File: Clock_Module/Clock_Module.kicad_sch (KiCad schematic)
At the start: 22 parts, among them SW1 SW_Wuerth_450301014042, U1 74LS08, U2 LM555xN, U3 LM555xN, U4 LM555xN, U5 74LS32, U6 74LS04

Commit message: Checkpoint: cleaned up clock module. Made one schematic. Good stop point
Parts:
- removed C3, C4, C6: .01µF, Capacitor_THT:C_Disc_D5.0mm_W2.5mm_P2.50mm, symbol Device:C
- removed D1: LED, LED_THT:LED_D5.0mm, symbol Device:LED
- removed Push1: SW_Push, Button_Switch_THT:SW_PUSH_6mm_H4.3mm, symbol Switch:SW_Push
- removed R3: 1M, Resistor_THT:R_Axial_DIN0207_L6.3mm_D2.5mm_P5.08mm_Vertical, symbol Device:R
- removed R4, R5, R6, R7: 1K, Resistor_THT:R_Axial_DIN0207_L6.3mm_D2.5mm_P5.08mm_Vertical, symbol Device:R
- removed SW1: SW_Wuerth_450301014042, MyFootPrints:SW_Slide-Jameco-SS-12E17-G020, symbol Switch:SW_Wuerth_450301014042
- removed U1: 74LS08, MyFootPrints:SN74LS08N, symbol 74xx:74LS08
- removed U2, U3, U4: LM555xN, Package_DIP:DIP-8_W7.62mm, symbol Timer:LM555xN
- removed U5: 74LS32, MyFootPrints:SN74LS32N, symbol 74xx:74LS32
- removed U6: 74LS04, MyFootPrints:SN74LS04N, symbol 74xx:74LS04
- added C10, C8, C9: .01µF, Capacitor_THT:C_Disc_D5.0mm_W2.5mm_P2.50mm, symbol Device:C
- added D2: LED, LED_THT:LED_D5.0mm, symbol Device:LED
- added J2: Barrel_Jack, symbol Connector:Barrel_Jack
- added Push2: SW_Push, Button_Switch_THT:SW_PUSH_6mm_H4.3mm, symbol Switch:SW_Push
- added R10, R11, R12, R14: 1K, Resistor_THT:R_Axial_DIN0207_L6.3mm_D2.5mm_P5.08mm_Vertical, symbol Device:R
- added R13: 1M, Resistor_THT:R_Axial_DIN0207_L6.3mm_D2.5mm_P5.08mm_Vertical, symbol Device:R
- added SW2: SW_Wuerth_450301014042, MyFootPrints:SW_Slide-Jameco-SS-12E17-G020, symbol Switch:SW_Wuerth_450301014042
- added U1, U11, U12: LM555xN, Package_DIP:DIP-8_W7.62mm, symbol Timer:LM555xN
- added U7: 74LS08, MyFootPrints:SN74LS08N, symbol 74xx:74LS08
- added U8: 74LS32, MyFootPrints:SN74LS32N, symbol 74xx:74LS32
- added U9: 74LS04, MyFootPrints:SN74LS04N, symbol 74xx:74LS04
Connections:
- net 5V: now also J2.1, R13.1, R14.2, SW2.1 (B), U1.4 (R), U1.8 (VCC), U11.8 (VCC), U12.4 (R), U12.8 (VCC), U7.14 (VCC), U8.14 (VCC), U9.14 (VCC)
- net CLK: now also D2.2 (A), U7.8, U9.5
- net GND: now also C10.1, C8.1, C9.1, J2.2, Push2.1, R10.1, R11.2, R12.2, U1.1 (GND), U1.5 (CV), U11.1 (GND), U11.6 (THR), U11.7 (DIS), U12.1 (GND), U7.7 (GND), U8.7 (GND), U9.7 (GND)
- net astable_out: now also U1.3 (Q), U7.1
- net bistable_out: now also U11.3 (Q), U7.2, U9.1
- net monostable_out: now also U12.3 (Q), U7.5
- net ~{CLK}: now also U9.6
- net at POT1.1: no longer R2.2
- net at POT1.2: now also R2.2
- net at C1.1, POT1.3: now also U1.2 (TR), U1.6 (THR)
- net at R1.1, R2.1: now also U1.7 (DIS)
- new net: D2.1 (K), R12.1
- new net: Push2.2, R14.1, U12.2 (TR)
- new net: U7.3, U8.1
- new net: U7.4, U9.2
- new net: R11.1, SW2.3 (A), U11.2 (TR)
- new net: R10.2, SW2.2 (C), U11.4 (R)
- new net: C8.2, U11.5 (CV)
- new net: U7.6, U8.2
- new net: U7.10, U9.4
- new net: C9.2, R13.2, U12.6 (THR), U12.7 (DIS)
- new net: C10.2, U12.5 (CV)
- new net: U7.9, U8.3
- new net halt: U9.3
- no-connect marks 20 -> 21
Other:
- note added: "Remove later"
- note removed: "Change to HLT"

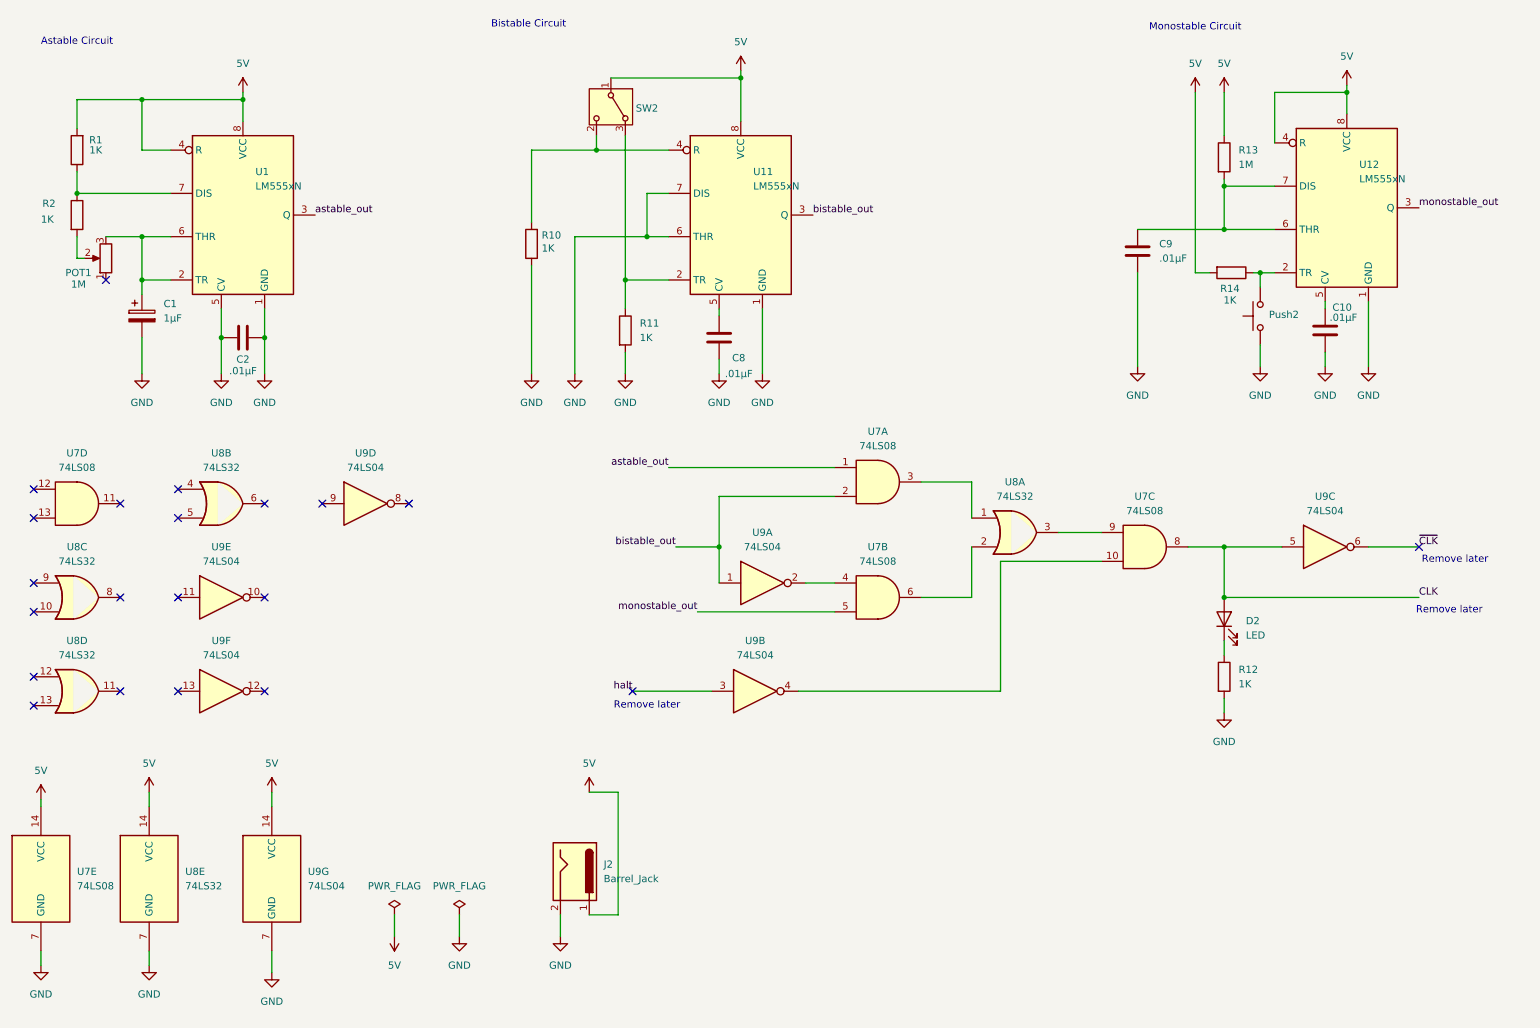
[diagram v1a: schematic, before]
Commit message: Updated Schematic to PC104 standards, updated Simulation for intel-quartus, updated PCB constraints, and edited board layout
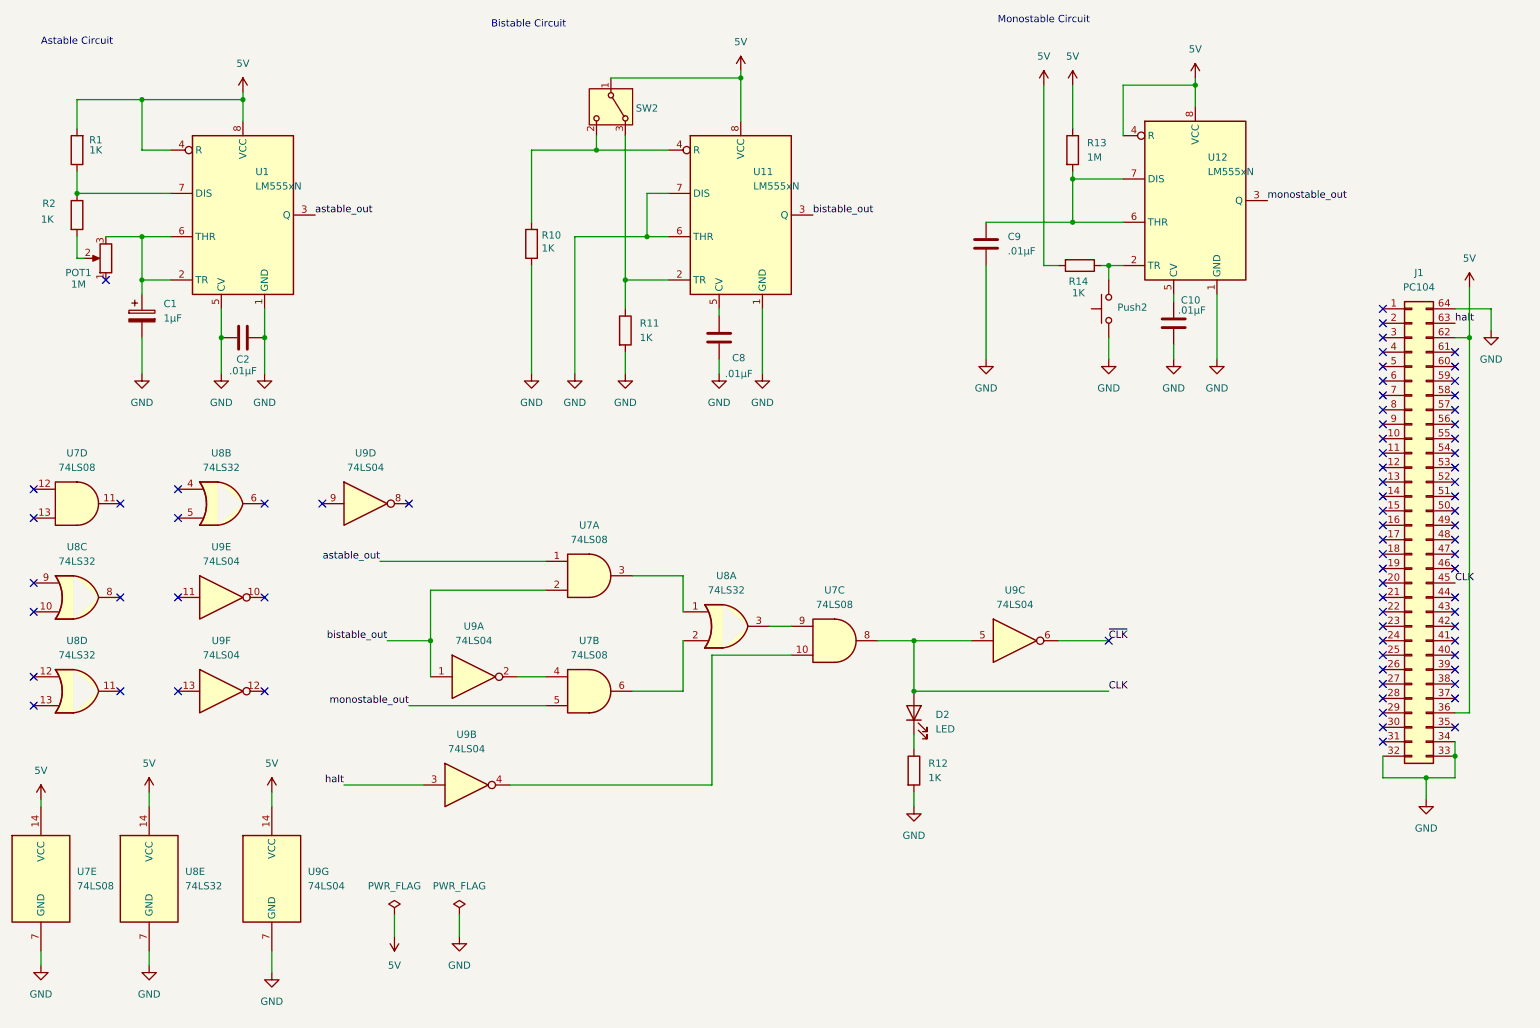
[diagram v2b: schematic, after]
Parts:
- removed J2: Barrel_Jack, symbol Connector:Barrel_Jack
- added J1: PC104, Connector_PinSocket_2.54mm:PinSocket_2x32_P2.54mm_Vertical, symbol Connector_Generic:Conn_02x32_Counter_Clockwise
- D2: footprint LED_THT:LED_D5.0mm -> LED_THT:LED_D5.0mm_Horizontal_O1.27mm_Z3.0mm
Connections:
- net 5V: now also J1.36 (Pin_36), J1.62 (Pin_62)
- net CLK: now also J1.45 (Pin_45)
- net GND: now also J1.32 (Pin_32), J1.33 (Pin_33), J1.34 (Pin_34), J1.64 (Pin_64)
- net halt: now also J1.63 (Pin_63)
- no-connect marks 21 -> 76
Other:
- note removed: "Remove later"
- moved on the sheet: C10, C9, D2, Push2, R12, R13, R14, U12, U7A, U7B, U7C, U8A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

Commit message: partially complete pcb and updated schematic with bypass capacitors
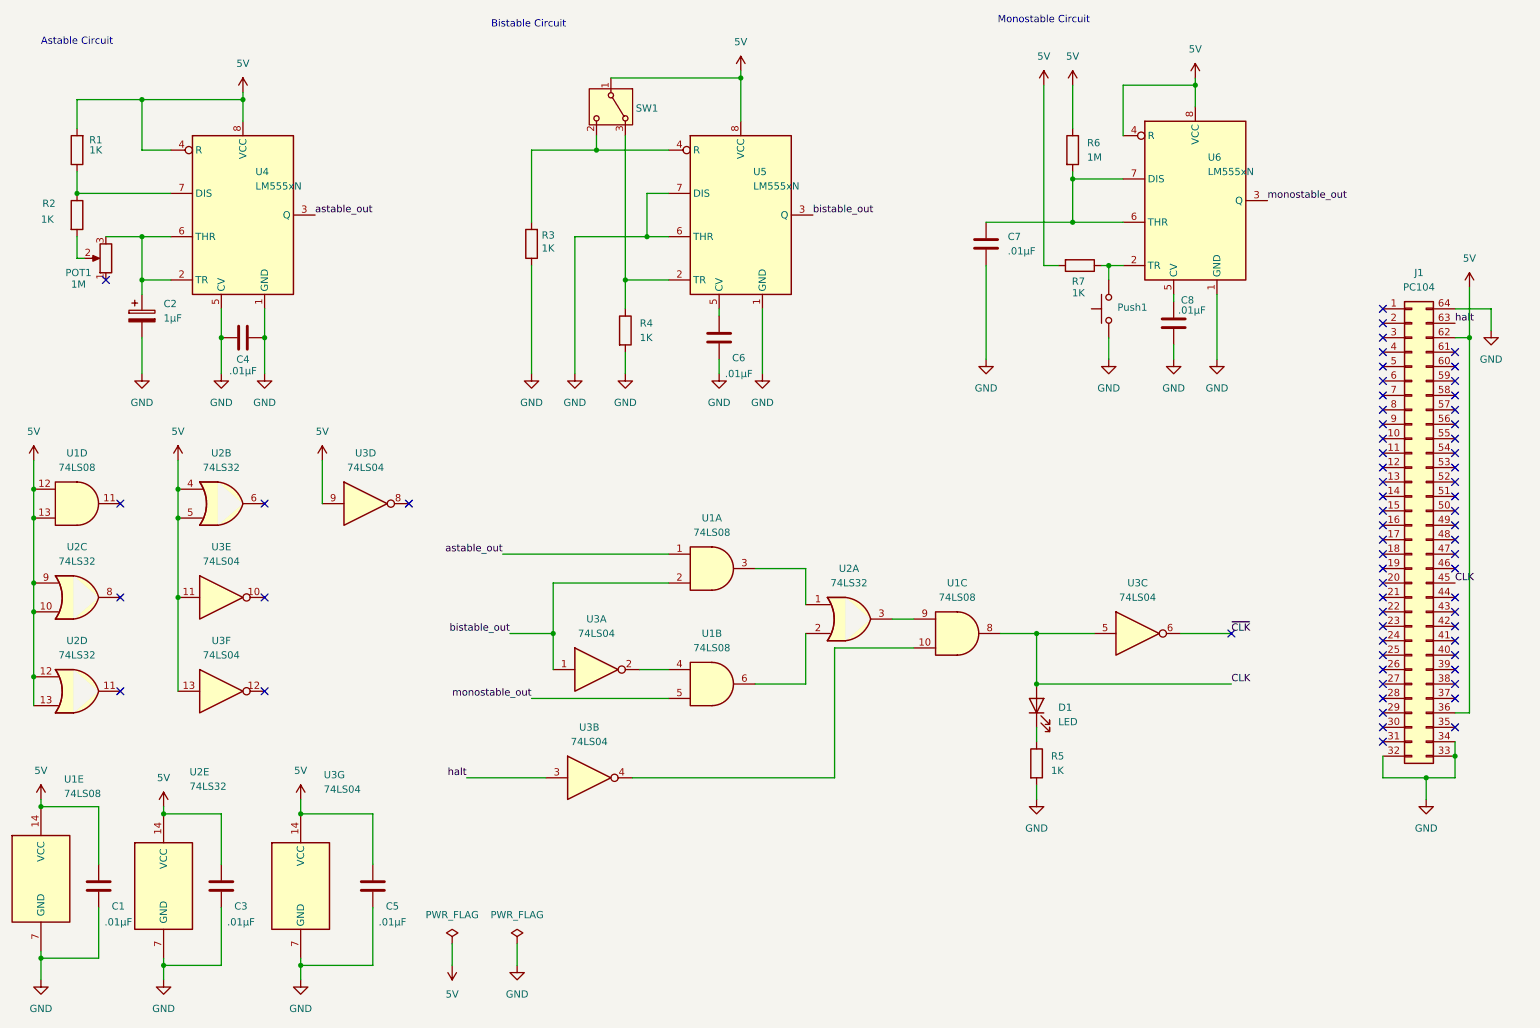
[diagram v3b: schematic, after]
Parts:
- added C1, C3, C5: .01µF, Capacitor_THT:C_Disc_D5.0mm_W2.5mm_P2.50mm, symbol Device:C
- SW1: renamed from SW2; value SW_Wuerth_450301014042 -> Switch
- renumbered C1 to C2, C2 to C4, C8 to C6, C9 to C7, C10 to C8, D2 to D1, Push2 to Push1, R10 to R3, R11 to R4, R12 to R5, R13 to R6, R14 to R7, U7 to U1, U8 to U2, U9 to U3, U1 to U4, U11 to U5, U12 to U6
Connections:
- net 5V: now also U1.12, U1.13, U2.10, U2.12, U2.13, U2.4, U2.5, U2.9, U3.11, U3.13, U3.9, C1.2, C3.2, C5.2
- net GND: now also C1.1, C3.1, C5.1
- no-connect marks 76 -> 65
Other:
- moved on the sheet: D1, R5, U1A, U1B, U1C, U2A, U2E, U3A, U3B, U3C, U3G

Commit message: Routed PCB
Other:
- company: (none) -> Arsenal Gear
- title: (none) -> Clock Module
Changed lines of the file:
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@@
 	(generator_version "8.0")
 	(paper "A4")
+	(title_block
+		(title "Clock Module")
+		(date "2024-10-22")
+		(rev ".10")
+		(company "Arsenal Gear")
+	)
 	(junction
 		(at 142.24 25.4)

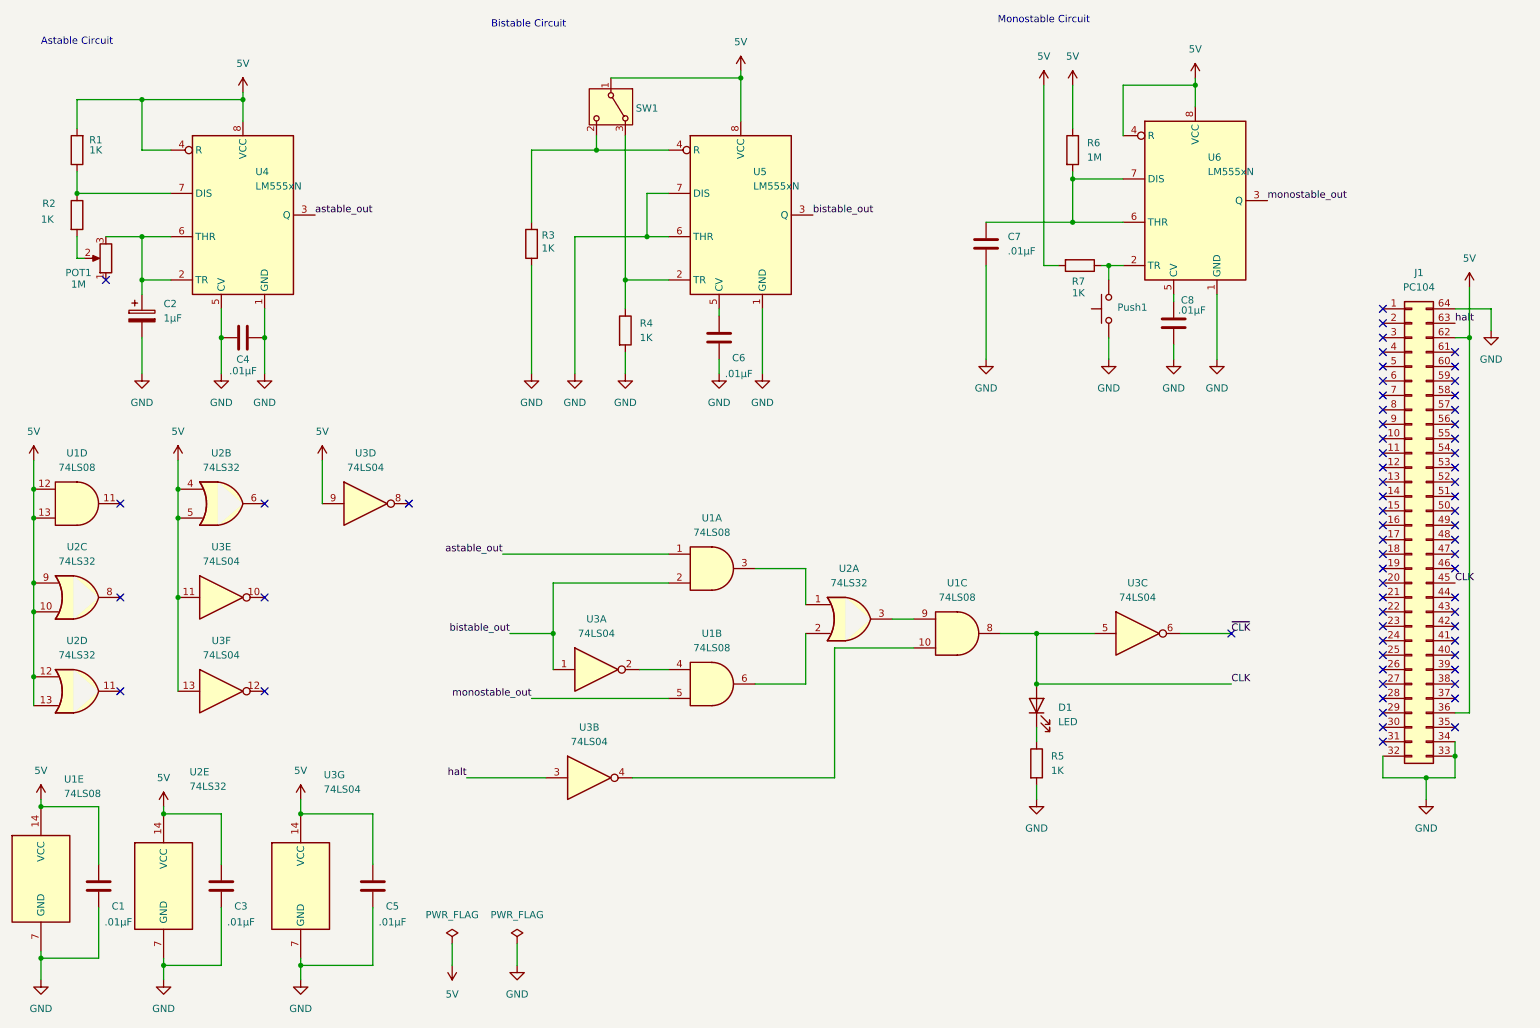
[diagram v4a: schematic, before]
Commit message: completed clock module
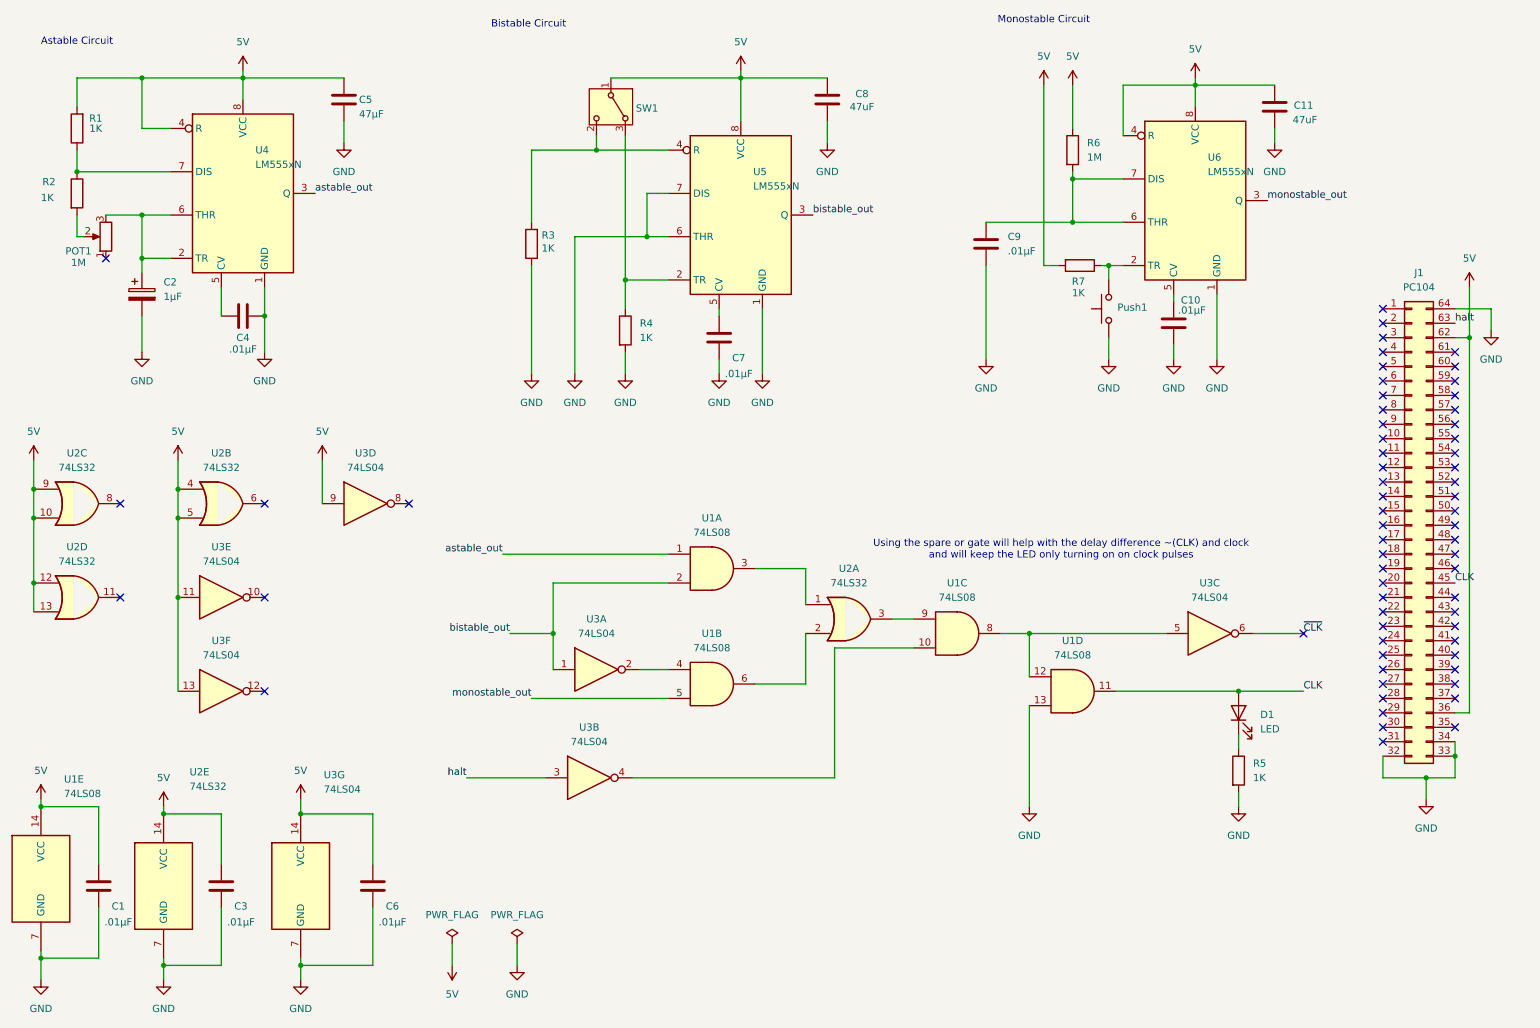
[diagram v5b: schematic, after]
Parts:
- added C11, C8: 47uF, Capacitor_THT:C_Disc_D5.0mm_W2.5mm_P2.50mm, symbol Device:C
- added C5: 47µF, Capacitor_THT:C_Disc_D5.0mm_W2.5mm_P2.50mm, symbol Device:C
- D1: footprint LED_THT:LED_D5.0mm_Horizontal_O1.27mm_Z3.0mm -> LED_THT:LED_D5.0mm
- renumbered C8 to C10, C5 to C6, C6 to C7, C7 to C9
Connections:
- net 5V: now also C11.1, C5.1, C8.2; no longer U1.12, U1.13
- net CLK: now also U1.11; no longer U1.8, U3.5
- net GND: now also U1.13, C11.2, C5.2, C8.1; no longer C4.2, U4.5 (CV)
- new net: C4.2, U4.5 (CV)
- new net: U1.12, U1.8, U3.5
- no-connect marks 65 -> 64
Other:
- note added: "Using the spare or gate will help with the delay difference ~(CLK) and clock and will keep the LED only turning on on clock pulses"
- moved on the sheet: C2, C4, D1, POT1, R1, R2, R5, U2C, U2D, U3C, U4
